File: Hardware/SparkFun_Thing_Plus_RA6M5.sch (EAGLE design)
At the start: 106 parts, among them J1 THING_PLUS_LOGICAL, J2 USB Female Type C Connector, J4 QWIIC_RA, J5 MICRO-SDFRICTION, J6 CONN_03X2, Q1 20V/4.2A/52mΩ/1.4W, Q2 20V/4.2A/52mΩ/1.4W, U1 RT9080-33GJ5, U2 MCP73831, U3 MAX17048, U4 R7FA6M5, U5 DA14531MOD, U6 W25QXX128MBIT-6X5, U7 MCP1501-3.3V, Y1 24.000MHz, Y2 32.768kHz

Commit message: Update Test Points, ready for v01 schematic review
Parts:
- removed C20: 2.2uF, SparkFun-Capacitors:2.2UF-0402_TIGHT-10V-10%-X5R
- removed R16: 2.2k, SparkFun-Resistors:2.2KOHM-0402T-1/16W-1%
- removed R17: 4.7k, SparkFun-Resistors:4.7KOHM-0402T-1/16W-1%
- removed TP10, TP11, TP12, TP13, TP14, TP15, TP16, TP17, TP18, TP19, TP20, TP21, TP22, TP23, TP24, TP9: TEST-POINT3X5, SparkFun-Connectors:TEST-POINT3X5
- added C15: 2.2uF, SparkFun-Capacitors:2.2UF-0402_TIGHT-10V-10%-X5R
- added R7: 2.2k, SparkFun-Resistors:2.2KOHM-0402T-1/16W-1%
- added R8: 10k, SparkFun-Resistors:10KOHM-0402T-1/16W-1%
- C1: value 2.2uF -> 1.0uF; device SparkFun-Capacitors:2.2UF-0402_TIGHT-10V-10%-X5R -> SparkFun-Capacitors:1.0UF-0402T-16V-10%
- C10, C9: value 0.1uF -> 12pF; device SparkFun-Capacitors:0.1UF-0402T-6.3V-10%-X7R -> SparkFun-Capacitors:12PF-0402T-50V-5%
- C13, C14: value 0.1uF -> 2.2uF; device SparkFun-Capacitors:0.1UF-0402T-6.3V-10%-X7R -> SparkFun-Capacitors:2.2UF-0402_TIGHT-10V-10%-X5R
- C16: value 1.0nF -> 2.2uF; device SparkFun-Capacitors:1.0NF/1000PF-0402_TIGHT-50V-10% -> SparkFun-Capacitors:2.2UF-0402_TIGHT-10V-10%-X5R
- C18: value 1.0uF -> 0.1uF; device SparkFun-Capacitors:1.0UF-0402T-16V-10% -> SparkFun-Capacitors:0.1UF-0402T-16V-10%
- C19: value 2.2uF -> 1.0nF; device SparkFun-Capacitors:2.2UF-0402_TIGHT-10V-10%-X5R -> SparkFun-Capacitors:1.0NF/1000PF-0402_TIGHT-50V-10%
- C2: value 2.2uF -> 0.1uF; device SparkFun-Capacitors:2.2UF-0402_TIGHT-10V-10%-X5R -> SparkFun-Capacitors:0.1UF-0402T-6.3V-10%-X7R
- C3: device SparkFun-Capacitors:0.1UF-0402T-16V-10% -> SparkFun-Capacitors:0.1UF-0402T-6.3V-10%-X7R
- C4, C5: value 12pF -> 0.1uF; device SparkFun-Capacitors:12PF-0402T-50V-5% -> SparkFun-Capacitors:0.1UF-0402T-6.3V-10%-X7R
- C6: value DNP -> 0.1uF; device SparkFun-Capacitors:DNP-0402-TIGHT_NO_CREAM -> SparkFun-Capacitors:0.1UF-0402T-6.3V-10%-X7R
- C8: value 0.1uF -> DNP; device SparkFun-Capacitors:0.1UF-0402T-6.3V-10%-X7R -> SparkFun-Capacitors:DNP-0402-TIGHT_NO_CREAM
- D2: value Yellow -> BLUE; device SparkFun-LED:LED-YELLOW0603 -> SparkFun-LED:LED-BLUE0603
- D4: value (none) -> WS2812_2020; device SparkFun-LED:LED-RED_0603-KB -> SparkFun-LED:WS2812_2020
- D5: value WS2812_2020 -> Yellow; device SparkFun-LED:WS2812_2020 -> SparkFun-LED:LED-YELLOW0603
- D6: value BLUE -> (none); device SparkFun-LED:LED-BLUE0603 -> SparkFun-LED:LED-RED_0603-KB
- J1: value THING_PLUS_LOGICAL -> USB Female Type C Connector; device SparkFun-Boards:THING_PLUS_LOGICAL -> SparkFun-Connectors:USB_C_4-LAYER-ISOLATED
- J2: value USB Female Type C Connector -> THING_PLUS_LOGICAL; device SparkFun-Connectors:USB_C_4-LAYER-ISOLATED -> SparkFun-Boards:THING_PLUS_LOGICAL
- J3: value (none) -> QWIIC_RA; device SparkFun-Connectors:JST_2MM_MALE -> SparkFun-Connectors:QWIIC_CONNECTORJS-1MM
- J4: value QWIIC_RA -> CONN_03X2; device SparkFun-Connectors:QWIIC_CONNECTORJS-1MM -> SparkFun_Thing_Plus_RA6M5:CONN_03X2
- J5: value MICRO-SDFRICTION -> (none); device SparkFun-Connectors:MICRO-SDFRICTION -> SparkFun-Connectors:SWD-5PIN
- J6: value CONN_03X2 -> (none); device SparkFun_Thing_Plus_RA6M5:CONN_03X2 -> SparkFun-Connectors:JST_2MM_MALE
- J7: value (none) -> MICRO-SDFRICTION; device SparkFun-Connectors:SWD-5PIN -> SparkFun-Connectors:MICRO-SDFRICTION
- LOGO1: value SFE_LOGO_NAME_FLAME.1_INCH -> OSHW-LOGOMINI; device SparkFun-Aesthetics:SFE_LOGO_NAME_FLAME.1_INCH -> SparkFun-Aesthetics:OSHW-LOGOMINI
- LOGO2: value QWIIC_LOGO_CONNECTOR -> SFE_LOGO_NAME_FLAME.1_INCH; device SparkFun-Aesthetics:QWIIC_LOGO_CONNECTOR -> SparkFun-Aesthetics:SFE_LOGO_NAME_FLAME.1_INCH
- LOGO3: value OSHW-LOGOMINI -> QWIIC_LOGO_CONNECTOR; device SparkFun-Aesthetics:OSHW-LOGOMINI -> SparkFun-Aesthetics:QWIIC_LOGO_CONNECTOR
- R1: value 4.7k -> 1k; device SparkFun-Resistors:4.7KOHM-0402T-1/16W-1% -> SparkFun-Resistors:1KOHM-0402T-1/16W-1%
- R11: value 20k -> 4.7k; device SparkFun-Resistors:20KOHM-0402T-1/16W-1% -> SparkFun-Resistors:4.7KOHM-0402T-1/16W-1%
- R12: value 10k -> 4.7k; device SparkFun-Resistors:10KOHM-0402T-1/16W-1% -> SparkFun-Resistors:4.7KOHM-0402T-1/16W-1%
- R2: value 4.7k -> 20k; device SparkFun-Resistors:4.7KOHM-0402T-1/16W-1% -> SparkFun-Resistors:20KOHM-0402T-1/16W-1%
- R9: value 1k -> 4.7k; device SparkFun-Resistors:1KOHM-0402T-1/16W-1% -> SparkFun-Resistors:4.7KOHM-0402T-1/16W-1%
- TP1, TP2, TP3, TP4, TP5, TP6, TP7, TP8: value TEST-POINT3X5 -> TEST-POINT3; device SparkFun-Connectors:TEST-POINT3X5 -> SparkFun-Connectors:TEST-POINT3
- U1: value RT9080-33GJ5 -> R7FA6M5; device SparkFun-IC-Power:V_REG_RT9080 -> SparkFun_Thing_Plus_RA6M5:R7FA6M5-100LQFP
- U2: value MCP73831 -> DA14531MOD; device SparkFun-IC-Power:MCP73831 -> SparkFun_Thing_Plus_RA6M5:DS14531MOD
- U3: value MAX17048 -> MCP73831; device SparkFun-IC-Power:MAX17048DFN8 -> SparkFun-IC-Power:MCP73831
- U4: value R7FA6M5 -> RT9080-33GJ5; device SparkFun_Thing_Plus_RA6M5:R7FA6M5-100LQFP -> SparkFun-IC-Power:V_REG_RT9080
- U5: value DA14531MOD -> W25QXX128MBIT-6X5; device SparkFun_Thing_Plus_RA6M5:DS14531MOD -> SparkFun-IC-Memory:W25QXX128MBIT-6X5
- U6: value W25QXX128MBIT-6X5 -> MCP1501-3.3V; device SparkFun-IC-Memory:W25QXX128MBIT-6X5 -> SparkFun_Thing_Plus_RA6M5:VREF-3.3V-0.1%
- U7: value MCP1501-3.3V -> MAX17048; device SparkFun_Thing_Plus_RA6M5:VREF-3.3V-0.1% -> SparkFun-IC-Power:MAX17048DFN8
- renumbered CHG to JP3, I2C to JP2, PWR to JP4, R13 to R10, SHLD to JP1
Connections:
- removed net VREF_EN: TP10.1
- net !CTS_RA6/RTS_DA14531!: now also TP7.1, U1G5.P303/CTS9/GTIOC7B, U2.P0_7/URTS; no longer TP23.1, U4G5.P303/CTS9/GTIOC7B, U5.P0_7/URTS
- net !FG_ALRT!: now also U1G7.P000/AN000/AN100, U7.!ALRT; no longer TP9.1, U3.!ALRT, U4G7.P000/AN000/AN100
- net !QCS!: now also RN1H.2, U1G6.P501/QSSL/TXD5/USB_OVRCURA, U5.!CS!; no longer RN4H.2, TP3.1, U4G6.P501/QSSL/TXD5/USB_OVRCURA, U6.!CS!
- net !RESET!: now also J2.!RESET, J4.6, U1G8.!RES!, U2.P0_11; no longer J1.!RESET, J6.6, U4G8.!RES!, U5.P0_11
- net !RTS_RA6/CTS_DA14531!: now also TP8.1, U1G5.P301/CTS9_RTS9/RXD2/SSLA2_B, U2.P0_8/UCTS; no longer TP24.1, U4G5.P301/CTS9_RTS9/RXD2/SSLA2_B, U5.P0_8/UCTS
- net 3.3V: now also C16.1, C2.1, C3.1, C4.1, C5.1, C6.1, D4.VCC, D6.A, J2.3.3V, J3.2, J4.1, J5.1, J7.VCC, RN1H.1, RN3C.1, RN3G.1, RN4A.1, U1G3.VBATT, U1G3.VCC, U1G3.VCC_USB, U2.V_BAT, U4.OUT, U5.VDD; no longer C10.1, C11.1, C12.1, C20.1, C8.1, C9.1, D4.A, D5.VCC, J1.3.3V, J4.2, J5.VCC, J6.1, J7.1, RN1C.1, RN1G.1, RN3A.1, RN4H.1, U1.OUT, U4G3.VBATT, U4G3.VCC, U4G3.VCC_USB, U5.V_BAT, U6.VDD
- net A0: now also J2.A0, U1G7.P014/AN012/DA0; no longer J1.A0, U4G7.P014/AN012/DA0
- net A1: now also J2.A1, U1G7.P015/AN013/DA1; no longer J1.A1, U4G7.P015/AN013/DA1
- net A2: now also J2.A2, U1G7.P505/AN121/RXD6/QIO3; no longer J1.A2, U4G7.P505/AN121/RXD6/QIO3
- net A3: now also J2.A3, U1G7.P504/AN120/USB_ID/QIO2/SCK6; no longer J1.A3, U4G7.P504/AN120/USB_ID/QIO2/SCK6
- net A4: now also J2.A4, U1G7.P503/AN119/USB_EXICEN/QIO1/SCK5; no longer J1.A4, U4G7.P503/AN119/USB_EXICEN/QIO1/SCK5
- net A5: now also J2.A5, U1G7.P502/AN118/USB_OVRCURB/QIO0/RXD5; no longer J1.A5, U4G7.P502/AN118/USB_OVRCURB/QIO0/RXD5
- net AGND: now also SUPPLYTIE1.P$1, U1G2.AVSS0, U1G2.VREFL, U1G2.VREFL0; no longer SUPPLYTIE3.P$1, U4G2.AVSS0, U4G2.VREFL, U4G2.VREFL0
- net AVCC0: now also TP4.1, U1G2.AVCC0; no longer TP19.1, U4G2.AVCC0
- net BOOT/MD: now also U1G8.P201/MD, U2.P0_9; no longer U4G8.P201/MD, U5.P0_9
- net DA14531_RST: now also TP3.1, U2.P0_0/RST; no longer TP11.1, U5.P0_0/RST
- net DA14531_SWCLK: now also J5.3, U2.P0_2/SWCLK; no longer J7.3, U5.P0_2/SWCLK
- net DA14531_SWDIO: now also J5.2, U2.P0_10/SWDIO; no longer J7.2, U5.P0_10/SWDIO
- net FREE: now also J2.FREEBIE, U1G1.P304/RXD6/GTOWLO/GTIOC7A; no longer J1.FREEBIE, U4G1.P304/RXD6/GTOWLO/GTIOC7A
- net GND: now also C1.1, C15.2, C3.2, C4.2, C5.2, C6.2, D4.GND, J3.1, J4.5, J5.5, J6.-, J7.GND, R5.1, R8.1, RN1C.1, RN1F.2, RN3A.1, RN4F.1, RN4G.1, RN4H.1, SUPPLYTIE1.P$2, SUPPLYTIE3.P$1, U1G3.VSS, U1G3.VSS_USB, U2.GND, U3.VSS, U4.GND, U7.CTG, U7.QSTRT; no longer C1.2, C10.2, C20.2, C3.1, C8.2, C9.2, D5.GND, J3.-, J4.1, J5.GND, J6.5, J7.5, R12.1, R16.1, RN1F.1, RN3C.1, RN3G.1, RN3H.1, RN4A.1, RN4F.2, SUPPLYTIE1.P$1, SUPPLYTIE3.P$2, U1.GND, U2.VSS, U3.CTG, U3.GND, U3.QSTRT, U4G3.VSS, U4G3.VSS_USB
- net GND_24: now also C8.1, SUPPLYTIE3.P$2; no longer C6.1, SUPPLYTIE1.P$2
- net GND_32: now also C10.1, C9.1; no longer C4.1, C5.1
- net GPIO0/!CS!: now also J2.GPIO0, U1G1.P112/SSLA0_B/TXD2/SCK1/QSSL; no longer J1.GPIO0, U4G1.P112/SSLA0_B/TXD2/SCK1/QSSL
- net GPIO1: now also J2.GPIO1, U1G9.P406/SSIRXD0_A/SSLA3_C; no longer J1.GPIO1, U4G9.P406/SSIRXD0_A/SSLA3_C
- net GPIO2: now also J2.GPIO2, U1G9.P405/SSITXD0_A/GTIOC1A; no longer J1.GPIO2, U4G9.P405/SSITXD0_A/GTIOC1A
- net GPIO3: now also J2.GPIO3, U1G9.P404/SSILRCK0_A/CTS7/RTCIC2; no longer J1.GPIO3, U4G9.P404/SSILRCK0_A/CTS7/RTCIC2
- net GPIO4: now also J2.GPIO4, U1G9.P403/SSIBCK0_A/CTS7_RTS7/RTCIC1; no longer J1.GPIO4, U4G9.P403/SSIBCK0_A/CTS7_RTS7/RTCIC1
- net GPIO5: now also J2.GPIO5, U1G9.P402/AUDIO_CLK/CTS4/RXD7/RTCIC0; no longer J1.GPIO5, U4G9.P402/AUDIO_CLK/CTS4/RXD7/RTCIC0
- net GPIO6: now also J2.GPIO6, U1G1.P207/TXD4/SSLA2_A/QSSL; no longer J1.GPIO6, U4G1.P207/TXD4/SSLA2_A/QSSL
- net N$1: now also R9.1; no longer R1.1
- net N$105: now also C10.2, U1G8.XCIN; no longer C4.2, U4G8.XCIN
- net N$108: now also C8.2, U1G8.P213/XTAL/TXD1; no longer C7.2, U4G8.P213/XTAL/TXD1
- net N$11: now also R7.2; no longer R5.2
- net N$110: now also C9.2, U1G8.XCOUT; no longer C5.2, U4G8.XCOUT
- net N$115: now also C7.2, U1G8.P212/EXTAL/RXD1; no longer C6.2, U4G8.P212/EXTAL/RXD1
- net N$12: now also RN3C.2, U1G1.P414/SDA2/CTS0/SSLB1_B/SD0WP; no longer RN1C.2, U4G1.P414/SDA2/CTS0/SSLB1_B/SD0WP
- net N$13: now also RN3A.2, U1G1.P708/AUDIO_CLK/RXD1/CECIO; no longer RN1A.2, U4G1.P708/AUDIO_CLK/RXD1/CECIO
- net N$14: now also R12.1; no longer R17.1
- net N$15: now also R2.2, RN3H.2, U1G5.P407/USB_VBUS/CTS4_RTS4; no longer R11.2, RN1H.2, U4G5.P407/USB_VBUS/CTS4_RTS4
- net N$16: now also D6.C, R12.2; no longer D4.C, R17.2
- net N$17: now also J1.D-; no longer J2.D-
- net N$18: now also RN1C.2, U1G1.P610/CRX1/CTS7/GTIOC5B/AGTO4; no longer RN4C.2, U4G1.P610/CRX1/CTS7/GTIOC5B/AGTO4
- net N$19: now also J1.SHLD; no longer J2.SHLD
- net N$2: now also D5.A; no longer D2.A
- net N$20: now also J1.CC2; no longer J2.CC2
- net N$21: now also J1.CC1; no longer J2.CC1
- net N$22: now also RN1B.2, U1G1.P609/CTX1/GTIOC5A/AGTO5; no longer RN4B.2, U4G1.P609/CTX1/GTIOC5A/AGTO5
- net N$23: now also RN1A.2, U1G1.P608/GTIOC4B; no longer RN4A.2, U4G1.P608/GTIOC4B
- net N$24: now also RN1D.2, U1G1.P600/SCK9/GTIOC6B; no longer RN4D.2, U4G1.P600/SCK9/GTIOC6B
- net N$25: now also RN3B.2, U1G1.P415/USB_VBUSEN/SCL2/SSLB2_B; no longer RN1B.2, U4G1.P415/USB_VBUSEN/SCL2/SSLB2_B
- net N$26: now also RN3D.2, U1G1.P413/CTS0_RTS0/SSLB0_B/SD0CLK_A; no longer RN1D.2, U4G1.P413/CTS0_RTS0/SSLB0_B/SD0CLK_A
- net N$27: now also RN3E.2, U1G1.P412/SCK0/CTS3/RSPCKB_B; no longer RN1E.2, U4G1.P412/SCK0/CTS3/RSPCKB_B
- net N$28: now also RN3F.2, U1G1.P411/TXD0/CTS3_RTS3/PICOB_B; no longer RN1F.2, U4G1.P411/TXD0/CTS3_RTS3/PICOB_B
- net N$29: now also RN4A.2, U1G8.P200/NMI; no longer RN3A.2, U4G8.P200/NMI
- net N$3: now also D5.C, U3.STAT; no longer D2.C, U2.STAT
- net N$30: now also RN4D.2, U1G1.P305/TXD6/QSPCLK/GTOWUP; no longer RN3D.2, U4G1.P305/TXD6/QSPCLK/GTOWUP
- net N$31: now also RN4E.2, U1G1.P302/TXD2/SSLA3_B/GTOUUP; no longer RN3E.2, U4G1.P302/TXD2/SSLA3_B/GTOUUP
- net N$32: now also RN4C.2, U1G1.P306/SCK6/QSSL/GTOULO_D; no longer RN3C.2, U4G1.P306/SCK6/QSSL/GTOULO_D
- net N$33: now also U1G1.P209/QIO2/SD0WP/GTOVUP; no longer U4G1.P209/QIO2/SD0WP/GTOVUP
- net N$34: now also RN4H.2, U1G1.P115/SSITXD0_B/GTIOC4A; no longer RN3H.2, U4G1.P115/SSITXD0_B/GTIOC4A
- net N$35: now also RN4G.2, U1G1.P114/CTS9/SSIRXD0_B/GTIOC2B; no longer RN3G.2, U4G1.P114/CTS9/SSIRXD0_B/GTIOC2B
- net N$36: now also RN4F.2, U1G1.P113/RXD2/SSILRCK0_B/GTIOC2A; no longer RN3F.2, U4G1.P113/RXD2/SSILRCK0_B/GTIOC2A
- net N$37: now also RN1E.2, U1G1.P107/CTS8_RTS8; no longer RN4E.2, U4G1.P107/CTS8_RTS8
- net N$38: now also RN1F.1, U1G7.P008/AN008; no longer RN4F.1, U4G7.P008/AN008
- net N$39: now also RN4B.2, U1G1.P307/CTS6_RTS6/QIO0/GTOUUP_D; no longer RN3B.2, U4G1.P307/CTS6_RTS6/QIO0/GTOUUP_D
- net N$41: now also U1G7.P007/AN007; no longer U4G7.P007/AN007
- net N$42: now also U1G7.P006/AN006; no longer U4G7.P006/AN006
- net N$43: now also U1G7.P005/AN005; no longer U4G7.P005/AN005
- net N$44: now also U1G7.P004/AN004; no longer U4G7.P004/AN004
- net N$45: now also U1G7.P003/AN003; no longer U4G7.P003/AN003
- net N$46: now also U1G7.P002/AN002/AN102; no longer U4G7.P002/AN002/AN102
- net N$47: now also U1G7.P001/AN001/AN101; no longer U4G7.P001/AN001/AN101
- net N$5: now also R11.2, U3.PROG; no longer R2.2, U2.PROG
- net N$6: now also D2.C, R5.2; no longer D6.C, R16.2
- net N$7: now also J1.D+; no longer J2.D+
- net N$8: now also J5.6; no longer J7.6
- net N$9: now also C1.2, R1.1, RN3H.1; no longer C18.2, R9.1, RN1H.1
- net N$97: now also C11.1, U1G3.VCL0; no longer C13.1, U4G3.VCL0
- net N$98: now also C12.1, U1G3.VCL; no longer C14.1, U4G3.VCL
- net QIO0: now also U1G6.P102/QIO0/SCK0/RSPCKB_A, U5.D0/DI; no longer TP5.1, U4G6.P102/QIO0/SCK0/RSPCKB_A, U6.D0/DI
- net QIO1: now also U1G6.P101/QIO1/TXD0/CTS1_RTS1/PICOB_A, U5.D1/DO; no longer TP6.1, U4G6.P101/QIO1/TXD0/CTS1_RTS1/PICOB_A, U6.D1/DO
- net QIO2: now also U1G6.P104/QIO2/RXD8/SSLB1_A, U5.D2/!WP!; no longer TP7.1, U4G6.P104/QIO2/RXD8/SSLB1_A, U6.D2/!WP!
- net QIO3: now also U1G6.P103/QIO3/SSLB0_A/CTS0_RTS0, U5.D3/!HOLD!; no longer TP8.1, U4G6.P103/QIO3/SSLB0_A/CTS0_RTS0, U6.D3/!HOLD!
- net QSPCLK: now also U1G6.P100/QSPCLK/RXD0/SCK1/POCIB_A, U5.CLK; no longer TP4.1, U4G6.P100/QSPCLK/RXD0/SCK1/POCIB_A, U6.CLK
- net RA6_SWCLK/TCK: now also J4.3, U1G6.P300/TCK/SWCLK/SSLA1_B; no longer J6.3, U4G6.P300/TCK/SWCLK/SSLA1_B
- net RA6_SWDIO/TMS: now also J4.2, U1G6.P108/TMS/SWDIO/CTS9_RTS9; no longer J6.2, U4G6.P108/TMS/SWDIO/CTS9_RTS9
- net RA6_SWO/TDO/PICO: now also J2.PICO, J4.4, U1G6.P109/TDO/SWO/PICOA_B/TXD9; no longer J1.PICO, J6.4, U4G6.P109/TDO/SWO/PICOA_B/TXD9
- net RA6_TDI/POCI: now also J2.POCI, U1G6.P110/TDI/POCIA_B/CTS2_RTS2/RXD9; no longer J1.POCI, U4G6.P110/TDI/POCIA_B/CTS2_RTS2/RXD9
- net RGB_DIN: now also D4.DI, U1G1.P105/TXD8/SSLB2_A; no longer D5.DI, TP1.1, U4G1.P105/TXD8/SSLB2_A
- net RGB_DOUT: now also D4.DO, TP1.1; no longer D5.DO, TP2.1
- net RX_RA6/TX_DA14531: now also TP6.1, U1G5.P601/RXD9/GTIOC6A, U2.P0_6/UTX; no longer TP22.1, U4G5.P601/RXD9/GTIOC6A, U5.P0_6/UTX
- net SCK: now also J2.SCK, U1G6.P111/RSPCKA_B/SCK2/SCK9; no longer J1.SCK, U4G6.P111/RSPCKA_B/SCK2/SCK9
- net SCL: now also J2.SCL, J3.4, R7.1, U1G5.P400/SCL0_A/SCK4/SCK7/AUDIO_CLK, U7.SCL; no longer J1.SCL, J4.4, R5.1, U3.SCL, U4G5.P400/SCL0_A/SCK4/SCK7/AUDIO_CLK
- net SDA: now also J2.SDA, J3.3, U1G5.P401/SDA0_A/TXD7/CTS4_RTS4, U7.SDA; no longer J1.SDA, J4.3, U3.SDA, U4G5.P401/SDA0_A/TXD7/CTS4_RTS4
- net SDCLK: now also J7.CLK/SCK, U1G4.P214/SD0CLK_B/QSPCLK; no longer J5.CLK/SCK, TP14.1, U4G4.P214/SD0CLK_B/QSPCLK
- net SDCMD: now also J7.CMD/SDI, U1G4.P211/SD0CMD_B/QIO0; no longer J5.CMD/SDI, TP13.1, U4G4.P211/SD0CMD_B/QIO0
- net SDDAT0: now also J7.DAT0/SDO, U1G4.P208/SD0DAT0_B/QIO3; no longer J5.DAT0/SDO, TP15.1, U4G4.P208/SD0DAT0_B/QIO3
- net SDDAT1: now also J7.DAT1, RN3G.2, U1G4.P410/SD0DAT1_A/RXD0/SCL2/SCK3; no longer J5.DAT1, RN1G.2, TP16.1, U4G4.P410/SD0DAT1_A/RXD0/SCL2/SCK3
- net SDDAT2: now also J7.DAT2, U1G4.P206/SD0DAT2_A/USB_VBUSEN/RXD4; no longer J5.DAT2, TP17.1, U4G4.P206/SD0DAT2_A/USB_VBUSEN/RXD4
- net SDDAT3: now also J7.DAT3/!CS!, U1G4.P205/SD0DAT3_A/TXD4/CTS9_RTS9; no longer J5.DAT3/!CS!, TP18.1, U4G4.P205/SD0DAT3_A/TXD4/CTS9_RTS9
- net SDDET: now also J7.DET, U1G4.P210/SD0CD/QIO1; no longer J5.DET, TP12.1, U4G4.P210/SD0CD/QIO1
- net STAT_LED: now also D2.A, U1G1.P106/SCK8/SSLB3_A; no longer D6.A, U4G1.P106/SCK8/SSLB3_A
- net TX_RA6/RX_DA14531: now also TP5.1, U1G5.P602/TXD9/GTIOC7B, U2.P0_5/URX; no longer TP21.1, U4G5.P602/TXD9/GTIOC7B, U5.P0_5/URX
- net UART_RX: now also J2.RX, U1G5.P408/RXD3/SCL0_B/USB_ID; no longer J1.RX, U4G5.P408/RXD3/SCL0_B/USB_ID
- net UART_TX: now also J2.TX, U1G5.P409/TXD3/SDA2/USB_EXICEN; no longer J1.TX, U4G5.P409/TXD3/SDA2/USB_EXICEN
- net USBD_N: now also U1G5.USB_DM; no longer U4G5.USB_DM
- net USBD_P: now also U1G5.USB_DP; no longer U4G5.USB_DP
- net VIN: now also C14.1, RN1G.1, U4.IN, U6.VDD; no longer C19.1, RN4G.1, U1.IN, U7.VDD
- net VREF1: now also C19.1, J2.AREF/NC, U1G2.VREFH, U1G2.VREFH0, U6.OUT; no longer C16.1, J1.AREF/NC, TP20.1, U4G2.VREFH, U4G2.VREFH0, U7.OUT
- net VREFEN: now also RN1G.2, TP2.1, U1G1.P500/USB_VBUSEN/CTS5/QSPCLK, U6.!SHDN!; no longer RN4G.2, U4G1.P500/USB_VBUSEN/CTS5/QSPCLK, U7.!SHDN!
- net VREG_EN: now also J2.EN, U4.EN; no longer J1.EN, U1.EN
- net V_BATT: now also C15.1, C18.2, J2.V_BATT, J6.+, U3.VBAT, U7.CELL, U7.VDD; no longer C2.1, C3.2, J1.V_BATT, J3.+, U2.VBAT, U3.CELL, U3.VDD
- net V_USB: now also C13.1, J1.VBUS, J2.V_USB, R8.2, U3.VIN; no longer C1.1, J1.V_USB, J2.VBUS, R12.2, U2.VIN
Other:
- moved on the sheet: C10, C11, C12, C4, C5, C6, C7, C8, C9, D2, D6, R12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

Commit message: Add documentation, update xtal caps.
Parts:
- C10, C9: value 12pF -> 9.1pF; device SparkFun-Capacitors:12PF-0402T-50V-5% -> SparkFun-Capacitors:9.1PF-0402-TIGHT
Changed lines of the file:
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@@
 <part name="GND18" library="SparkFun-PowerSymbols" deviceset="GND" device="" value="GND_24"/>
 <part name="GND19" library="SparkFun-PowerSymbols" deviceset="GND" device="" value="GND_32"/>
-<part name="C10" library="SparkFun-Capacitors" deviceset="12PF" device="-0402T-50V-5%" value="12pF"/>
-<part name="C9" library="SparkFun-Capacitors" deviceset="12PF" device="-0402T-50V-5%" value="12pF"/>
+<part name="C10" library="SparkFun-Capacitors" deviceset="9.1PF" device="-0402-TIGHT" value="9.1pF"/>
+<part name="C9" library="SparkFun-Capacitors" deviceset="9.1PF" device="-0402-TIGHT" value="9.1pF"/>
 <part name="SUPPLYTIE3" library="SparkFun_Thing_Plus_RA6M5" deviceset="2PT_GND_TIE" device="SMALL"/>
 <part name="SUPPLYTIE2" library="SparkFun_Thing_Plus_RA6M5" deviceset="2PT_GND_TIE" device="SMALL"/>

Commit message: Made board 6L and created 6L Isolated USB
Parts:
- added H3, H4: STAND-OFFTIGHT, SparkFun-Hardware:STAND-OFFTIGHT
- J1: device SparkFun-Connectors:USB_C_4-LAYER-ISOLATED -> SparkFun_Thing_Plus_RA6M5:USB_C_6-LAYER-ISOLATED
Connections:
- net !QCS!: now also RN1G.2; no longer RN1H.2
- net 3.3V: now also RN1G.1; no longer RN1H.1
- net VIN: now also RN1H.1; no longer RN1G.1
- net VREFEN: now also RN1H.2; no longer RN1G.2
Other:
- moved on the sheet: RN1G, RN1H
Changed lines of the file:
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@@
 <layer number="1" name="Top" color="4" fill="1" visible="no" active="no"/>
 <layer number="2" name="Route2" color="1" fill="3" visible="no" active="no"/>
+<layer number="3" name="Route3" color="4" fill="3" visible="no" active="no"/>
+<layer number="4" name="Route4" color="1" fill="4" visible="no" active="no"/>
+<layer number="5" name="Route5" color="4" fill="4" visible="no" active="no"/>
+<layer number="6" name="Route6" color="1" fill="8" visible="no" active="no"/>
+<layer number="7" name="Route7" color="4" fill="8" visible="no" active="no"/>
+<layer number="8" name="Route8" color="1" fill="2" visible="no" active="no"/>
+<layer number="9" name="Route9" color="4" fill="2" visible="no" active="no"/>
+<layer number="10" name="Route10" color="1" fill="7" visible="no" active="no"/>
+<layer number="11" name="Route11" color="4" fill="7" visible="no" active="no"/>
+<layer number="12" name="Route12" color="1" fill="5" visible="no" active="no"/>
+<layer number="13" name="Route13" color="4" fill="5" visible="no" active="no"/>
+<layer number="14" name="Route14" color="1" fill="6" visible="no" active="no"/>
 <layer number="15" name="Route15" color="4" fill="6" visible="no" active="no"/>
 <layer number="16" name="Bottom" color="1" fill="1" visible="no" active="no"/>
@@
 <part name="SUPPLY3" library="SparkFun-PowerSymbols" deviceset="3.3V" device=""/>
 <part name="GND1" library="SparkFun-PowerSymbols" deviceset="GND" device=""/>
-<part name="J1" library="SparkFun-Connectors" deviceset="USB_C" device="_4-LAYER-ISOLATED" value="USB Female Type C Connector"/>
+<part name="J1" library="SparkFun_Thing_Plus_RA6M5" deviceset="USB_C" device="_6-LAYER-ISOLATED" value="USB Female Type C Connector"/>
 <part name="D1" library="SparkFun-IC-Power" deviceset="PRTR5V0U2" device="F"/>
 <part name="U4" library="SparkFun-IC-Power" deviceset="V_REG_RT9080" device="" value="RT9080-33GJ5"/>
@@
 <part name="TP7" library="SparkFun-Connectors" deviceset="TEST-POINT" device="3" value="TEST-POINT3"/>
 <part name="TP8" library="SparkFun-Connectors" deviceset="TEST-POINT" device="3" value="TEST-POINT3"/>
+<part name="H3" library="SparkFun-Hardware" deviceset="STAND-OFF" device="TIGHT"/>
+<part name="H4" library="SparkFun-Hardware" deviceset="STAND-OFF" device="TIGHT"/>
 </parts>
 <sheets>
@@
 <attribute name="VALUE" x="332.74" y="108.966" size="1.778" layer="96" font="vector" align="top-center"/>
 </instance>
+<instance part="H3" gate="G$1" x="429.26" y="27.94" smashed="yes"/>
+<instance part="H4" gate="G$1" x="426.72" y="27.94" smashed="yes"/>
 </instances>
 <busses>
@@
 <attribute name="VALUE" x="270.256" y="35.56" size="1.778" layer="96" font="vector" rot="R270" align="top-center"/>
 </instance>
-<instance part="RN1" gate="H" x="396.24" y="101.6" smashed="yes" rot="R270">
-<attribute name="NAME" x="397.764" y="101.6" size="1.778" layer="95" font="vector" rot="R270" align="bottom-center"/>
-<attribute name="VALUE" x="394.716" y="101.6" size="1.778" layer="96" font="vector" rot="R270" align="top-center"/>
+<instance part="RN1" gate="H" x="363.22" y="233.68" smashed="yes">
+<attribute name="NAME" x="363.22" y="235.204" size="1.778" layer="95" font="vector" align="bottom-center"/>
+<attribute name="VALUE" x="363.22" y="232.156" size="1.778" layer="96" font="vector" align="top-center"/>
 </instance>
 <instance part="RN5" gate="A" x="398.78" y="170.18" smashed="yes" rot="R90">
@@
 <attribute name="VALUE" x="400.304" y="170.18" size="1.778" layer="96" font="vector" rot="R90" align="top-center"/>
 </instance>
-<instance part="RN1" gate="G" x="363.22" y="233.68" smashed="yes">
-<attribute name="NAME" x="363.22" y="235.204" size="1.778" layer="95" font="vector" align="bottom-center"/>
-<attribute name="VALUE" x="363.22" y="232.156" size="1.778" layer="96" font="vector" align="top-center"/>
+<instance part="RN1" gate="G" x="396.24" y="101.6" smashed="yes" rot="R270">
+<attribute name="NAME" x="397.764" y="101.6" size="1.778" layer="95" font="vector" rot="R270" align="bottom-center"/>
+<attribute name="VALUE" x="394.716" y="101.6" size="1.778" layer="96" font="vector" rot="R270" align="top-center"/>
 </instance>
 <instance part="SUPPLY40" gate="G$1" x="396.24" y="109.22" smashed="yes">
@@
 </segment>
 <segment>
+<pinref part="RN1" gate="G" pin="1"/>
 <pinref part="SUPPLY40" gate="G$1" pin="3.3V"/>
-<pinref part="RN1" gate="H" pin="1"/>
-<wire x1="396.24" y1="109.22" x2="396.24" y2="106.68" width="0.1524" layer="91"/>
+<wire x1="396.24" y1="106.68" x2="396.24" y2="109.22" width="0.1524" layer="91"/>
 </segment>
 </net>
@@
 <junction x="355.6" y="228.6"/>
 <wire x1="355.6" y1="236.22" x2="355.6" y2="233.68" width="0.1524" layer="91"/>
-<pinref part="RN1" gate="G" pin="1"/>
+<pinref part="RN1" gate="H" pin="1"/>
 <wire x1="355.6" y1="233.68" x2="355.6" y2="228.6" width="0.1524" layer="91"/>
 <wire x1="358.14" y1="233.68" x2="355.6" y2="233.68" width="0.1524" layer="91"/>
@@
 <net name="!QCS!" class="0">
 <segment>
-<wire x1="398.78" y1="93.98" x2="396.24" y2="93.98" width="0.1524" layer="91"/>
 <label x="398.78" y="93.98" size="1.27" layer="95" font="vector" rot="MR180" xref="yes"/>
 <pinref part="U5" gate="U1" pin="!CS!"/>
-<pinref part="RN1" gate="H" pin="2"/>
+<wire x1="398.78" y1="93.98" x2="396.24" y2="93.98" width="0.1524" layer="91"/>
+<pinref part="RN1" gate="G" pin="2"/>
 <wire x1="396.24" y1="93.98" x2="393.7" y2="93.98" width="0.1524" layer="91"/>
 <wire x1="396.24" y1="96.52" x2="396.24" y2="93.98" width="0.1524" layer="91"/>
@@
 <wire x1="370.84" y1="238.76" x2="370.84" y2="233.68" width="0.1524" layer="91"/>
 <label x="368.3" y="238.76" size="1.27" layer="95" font="vector" rot="R180" xref="yes"/>
-<pinref part="RN1" gate="G" pin="2"/>
+<pinref part="RN1" gate="H" pin="2"/>
 <wire x1="368.3" y1="233.68" x2="370.84" y2="233.68" width="0.1524" layer="91"/>
 <junction x="370.84" y="233.68"/>

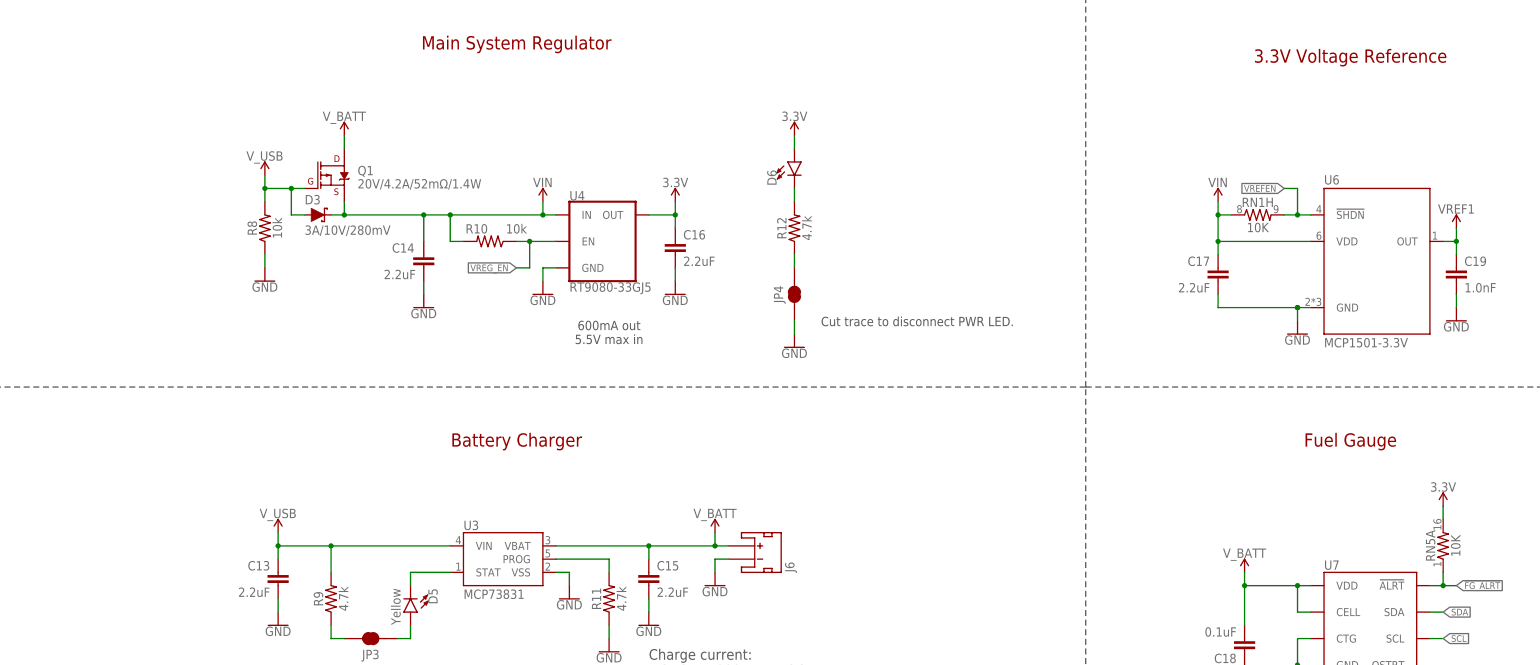
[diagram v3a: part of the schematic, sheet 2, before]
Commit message: Added LM66200 and incorporated it.
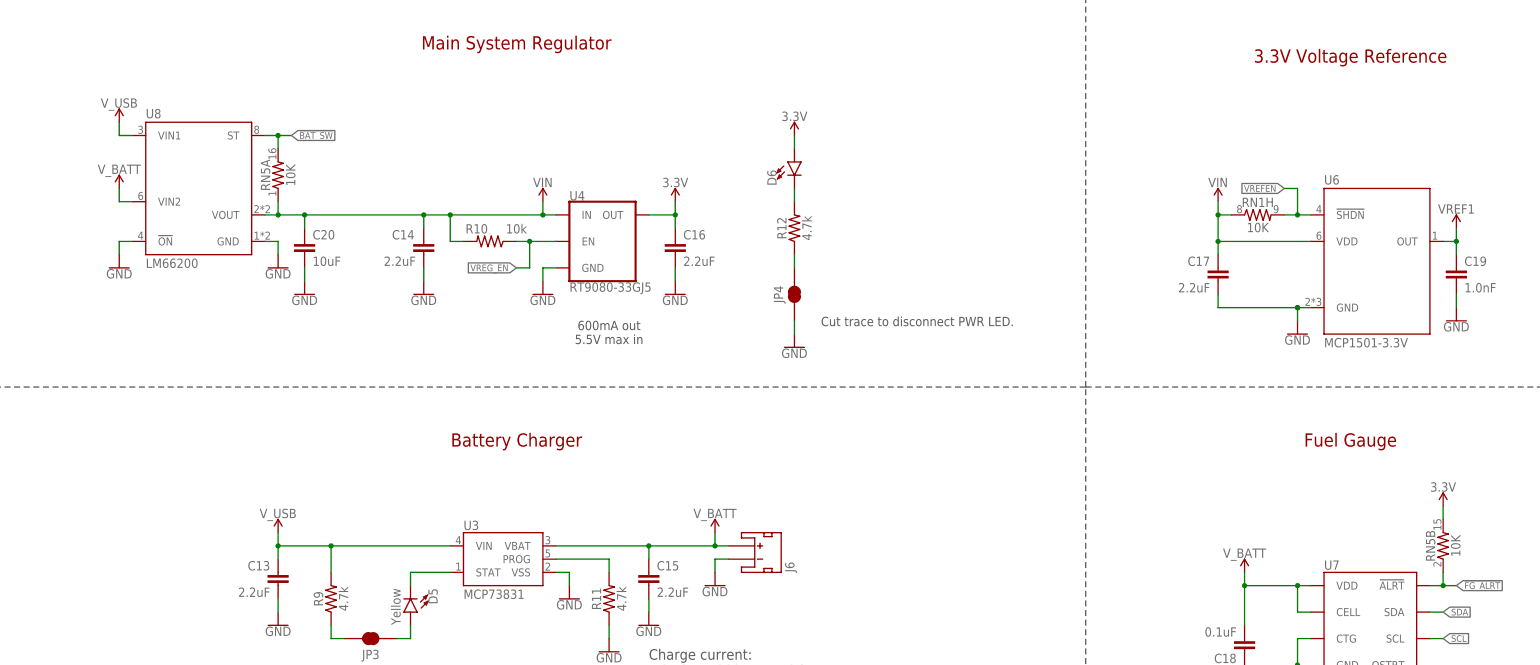
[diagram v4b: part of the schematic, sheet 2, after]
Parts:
- removed D3: 3A/10V/280mV, SparkFun-DiscreteSemi:DIODE-SCHOTTKY-BAT60A
- removed Q1: 20V/4.2A/52mΩ/1.4W, SparkFun-DiscreteSemi:MOSFET_PCH-DMG2305UX-7
- removed R8: 10k, SparkFun-Resistors:10KOHM-0402T-1/16W-1%
- added C20: 10uF, SparkFun-Capacitors:10UF-0805-25V-10%
- added U8: LM66200, SparkFun_Thing_Plus_RA6M5:IDEAL_DIODE_DUAL_LM66200
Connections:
- removed net N$47: RN5B.1, U1G7.P001/AN001/AN101
- new net !BAT_SW!: RN5A.2, U1G7.P001/AN001/AN101, U8.ST
- net !FG_ALRT!: now also RN5B.1; no longer RN5A.1
- net 3.3V: now also RN5B.2; no longer RN5A.2
- net GND: now also C20.2, U8.!ON!, U8.GND; no longer R8.1, RN5B.2
- net VIN: now also C20.1, RN5A.1, U8.VOUT; no longer D3.C, Q1.S
- net V_BATT: now also U8.VIN2; no longer Q1.D
- net V_USB: now also U8.VIN1; no longer D3.A, Q1.G, R8.2
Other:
- moved on the sheet: C14, RN5A
